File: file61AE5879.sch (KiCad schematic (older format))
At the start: 7 parts, among them U1 8086_Min_Mode, U2 74LS245, U3 74LS245, U4 74LS373, U5 74LS373, U6 74LS373

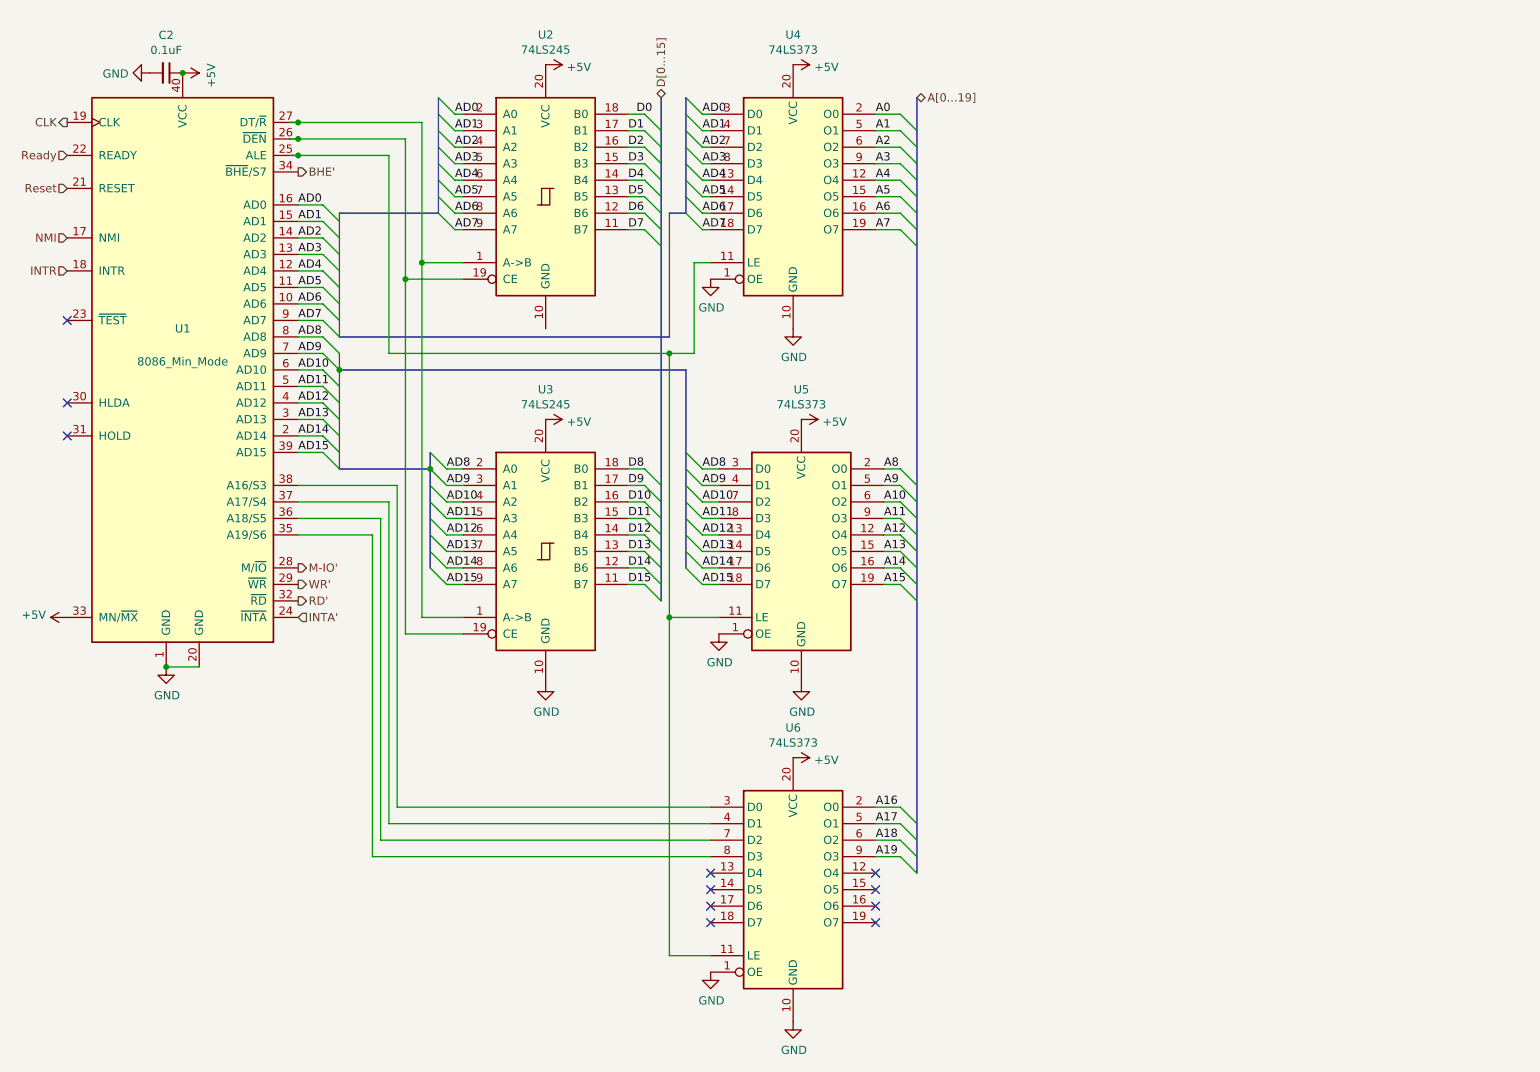
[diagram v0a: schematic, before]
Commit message: Added external headers
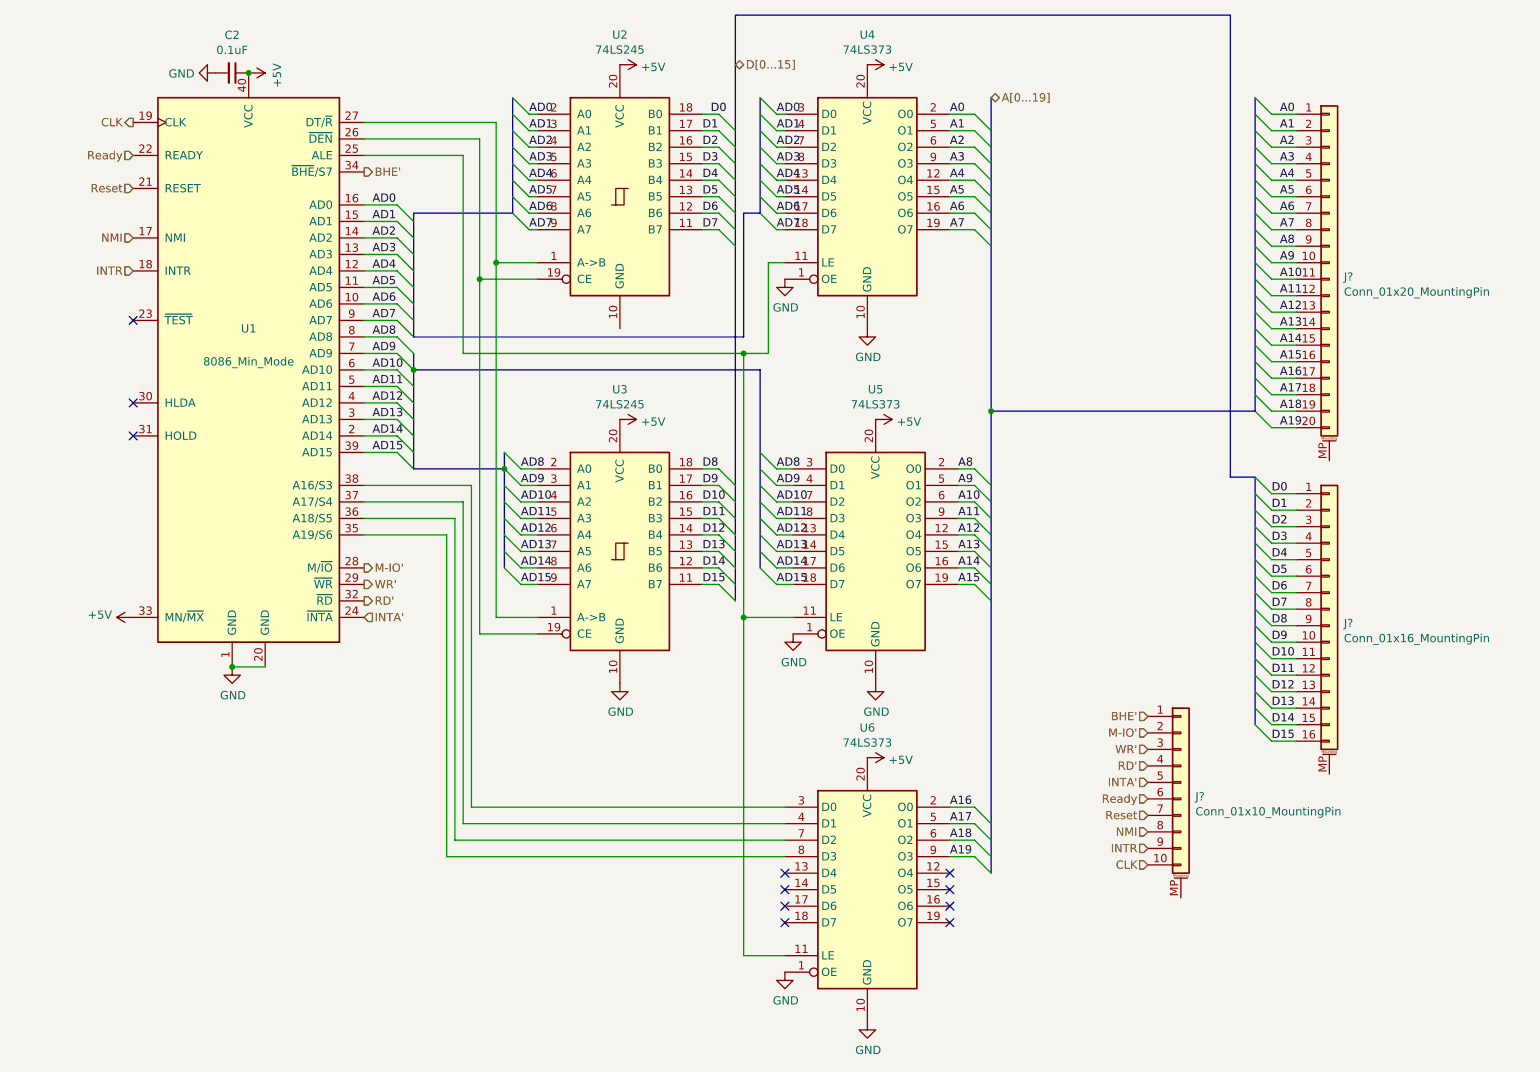
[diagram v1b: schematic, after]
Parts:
- added J?: Conn_01x20_MountingPin, symbol Connector_Generic_MountingPin:Conn_01x20_MountingPin
- added J?: Conn_01x16_MountingPin, symbol Connector_Generic_MountingPin:Conn_01x16_MountingPin
- added J?: Conn_01x10_MountingPin, symbol Connector_Generic_MountingPin:Conn_01x10_MountingPin
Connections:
- net A0: now also J?.1 (Pin_1)
- net A1: now also J?.2 (Pin_2)
- net A10: now also J?.11 (Pin_11)
- net A11: now also J?.12 (Pin_12)
- net A12: now also J?.13 (Pin_13)
- net A13: now also J?.14 (Pin_14)
- net A14: now also J?.15 (Pin_15)
- net A15: now also J?.16 (Pin_16)
- net A16: now also J?.17 (Pin_17)
- net A17: now also J?.18 (Pin_18)
- net A18: now also J?.19 (Pin_19)
- net A19: now also J?.20 (Pin_20)
- net A2: now also J?.3 (Pin_3)
- net A3: now also J?.4 (Pin_4)
- net A4: now also J?.5 (Pin_5)
- net A5: now also J?.6 (Pin_6)
- net A6: now also J?.7 (Pin_7)
- net A7: now also J?.8 (Pin_8)
- net A8: now also J?.9 (Pin_9)
- net A9: now also J?.10 (Pin_10)
- net BHE': now also J?.1 (Pin_1)
- net CLK: now also J?.10 (Pin_10)
- net D0: now also J?.1 (Pin_1)
- net D1: now also J?.2 (Pin_2)
- net D10: now also J?.11 (Pin_11)
- net D11: now also J?.12 (Pin_12)
- net D12: now also J?.13 (Pin_13)
- net D13: now also J?.14 (Pin_14)
- net D14: now also J?.15 (Pin_15)
- net D15: now also J?.16 (Pin_16)
- net D2: now also J?.3 (Pin_3)
- net D3: now also J?.4 (Pin_4)
- net D4: now also J?.5 (Pin_5)
- net D5: now also J?.6 (Pin_6)
- net D6: now also J?.7 (Pin_7)
- net D7: now also J?.8 (Pin_8)
- net D8: now also J?.9 (Pin_9)
- net D9: now also J?.10 (Pin_10)
- net INTA': now also J?.5 (Pin_5)
- net INTR: now also J?.9 (Pin_9)
- net M-IO': now also J?.2 (Pin_2)
- net NMI: now also J?.8 (Pin_8)
- net RD': now also J?.4 (Pin_4)
- net Ready: now also J?.6 (Pin_6)
- net Reset: now also J?.7 (Pin_7)
- net WR': now also J?.3 (Pin_3)
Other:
- moved on the sheet: C2, U1, U2, U3, U4, U5, U6

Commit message: Fixing Weirdness
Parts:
- removed J?: Conn_01x20_MountingPin, symbol Connector_Generic_MountingPin:Conn_01x20_MountingPin
- removed J?: Conn_01x16_MountingPin, symbol Connector_Generic_MountingPin:Conn_01x16_MountingPin
- removed J?: Conn_01x10_MountingPin, symbol Connector_Generic_MountingPin:Conn_01x10_MountingPin
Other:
- moved on the sheet: C2, U1, U2, U3, U4, U5, U6
